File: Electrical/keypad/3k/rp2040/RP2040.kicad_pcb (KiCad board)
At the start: 4 copper layers, 67.8 x 67.7 mm, 77 parts, among them J1 Conn_01x04_Socket, P1 USB-TYPE-C-016, Q1 BSS138, SW1 TS-1187A-B-A-B, SW2 TS-1187A-B-A-B, SW3 BUTT1, SW4 BUTT3, SW5 BUTT2, U1 PRTR5V0U2X, U2 ME6208A44M3G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

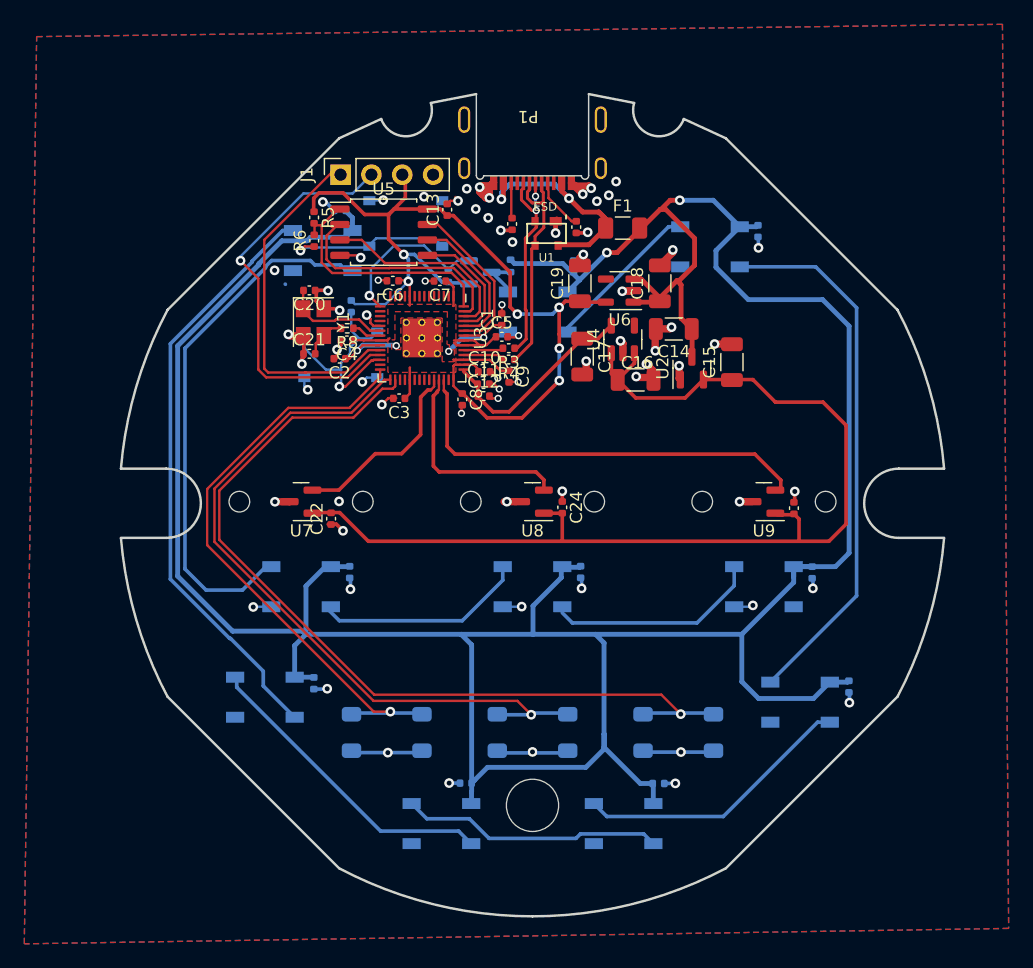
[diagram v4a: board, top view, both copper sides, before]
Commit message: finishes new pcb edge cuts
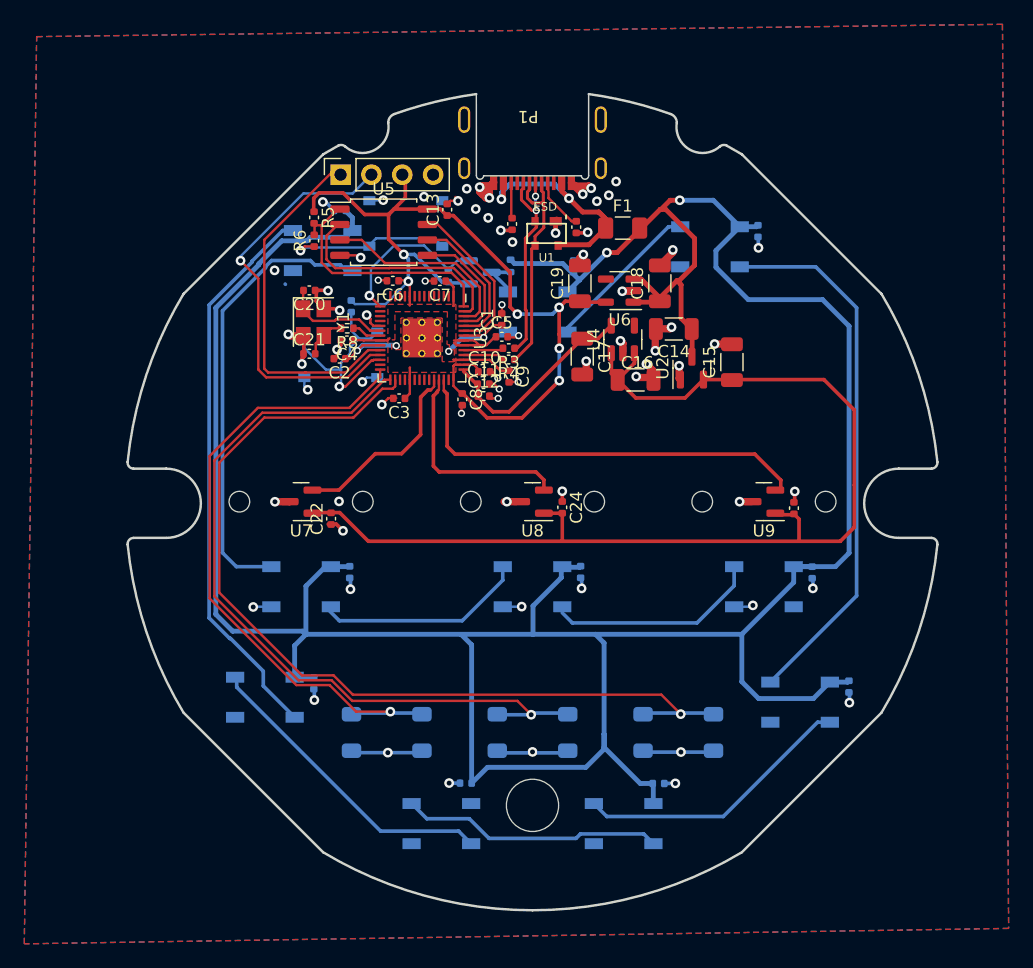
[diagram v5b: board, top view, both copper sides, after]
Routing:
- net UG_DIN: track 43.5 -> 36.8 mm
- net +5V: track 266.1 -> 260.6 mm
- net BUTT1: track 59.9 -> 63.9 mm
- net BUTT2: track 71.9 -> 75.8 mm
- net BUTT0: track 49.4 -> 53.2 mm
- net Net-(D10-DIN): track 49.0 -> 46.4 mm
- net +4V4: track 88.7 -> 90.7 mm
- net GND: track 89.9 -> 89.4 mm
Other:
- board size 67.8 x 67.7 mm -> 66.7 x 67.2 mm

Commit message: adds stitching vias
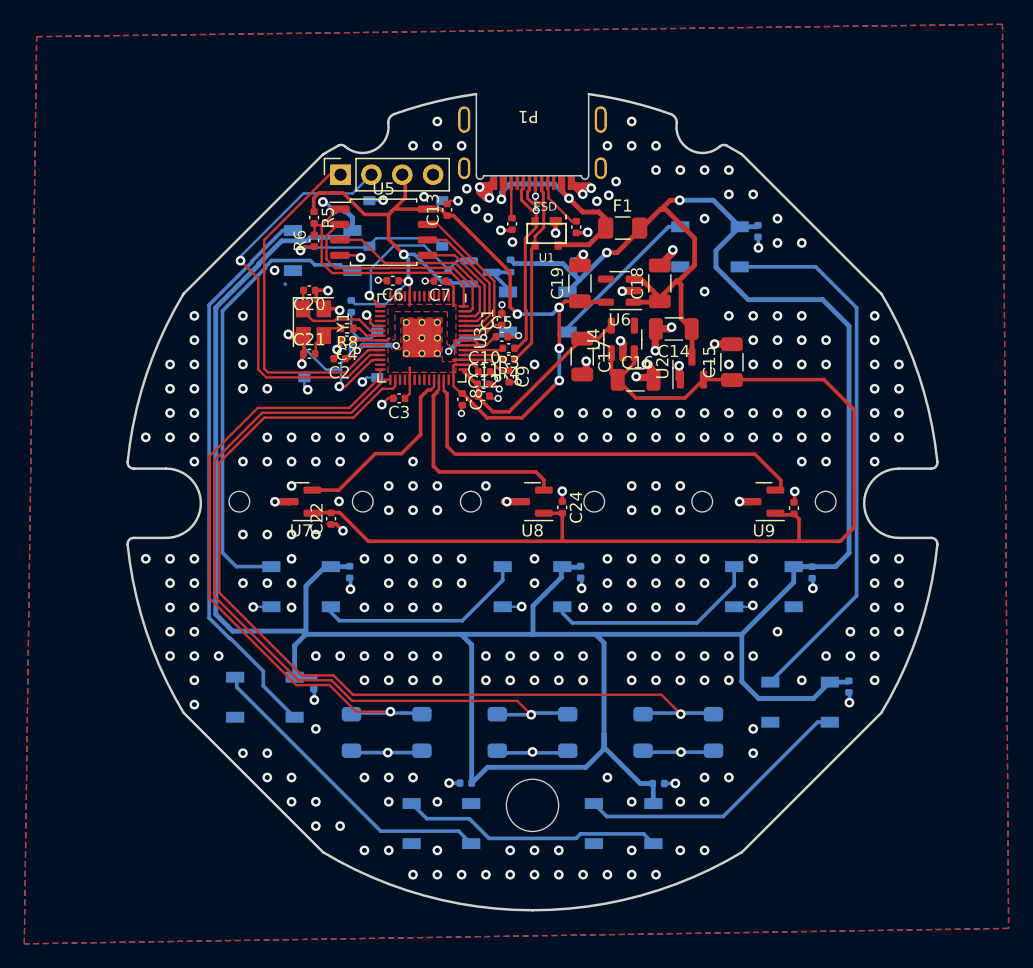
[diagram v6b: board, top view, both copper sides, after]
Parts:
- SW4: value BUTT3 -> BUTT2
- SW5: value BUTT2 -> BUTT3
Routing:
- net GND: vias 70 -> 330
